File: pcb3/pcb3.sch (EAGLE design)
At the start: 31 parts, among them J1 12V, J2 24V, J3 RTD, J4 RTD, J5 VFS, J6 RELAY, J7 BRAKES, Q1 BSS314PEH6327XTSA1, Q2 BSS314PEH6327XTSA1, Q3 MMBT2222AT-7-F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

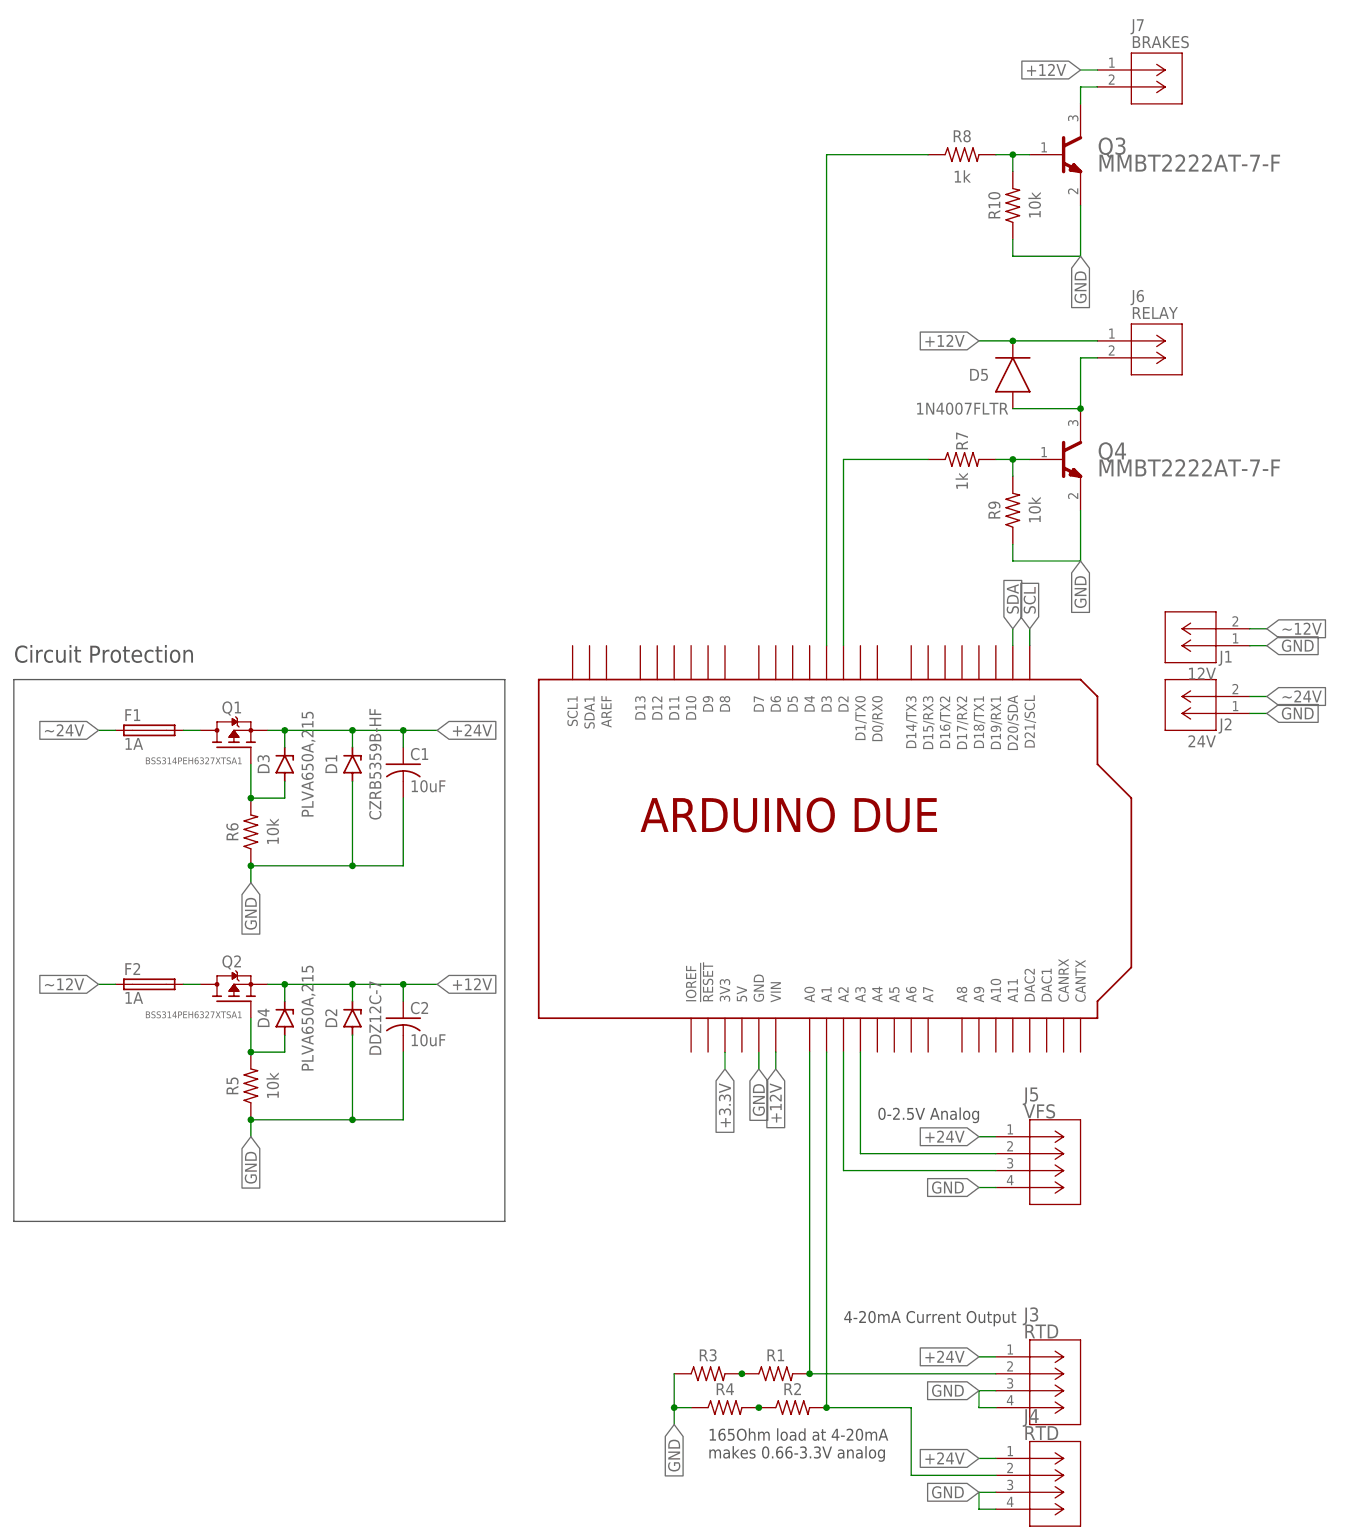
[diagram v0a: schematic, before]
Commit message: Add Serial CAN Bus to PCB 3
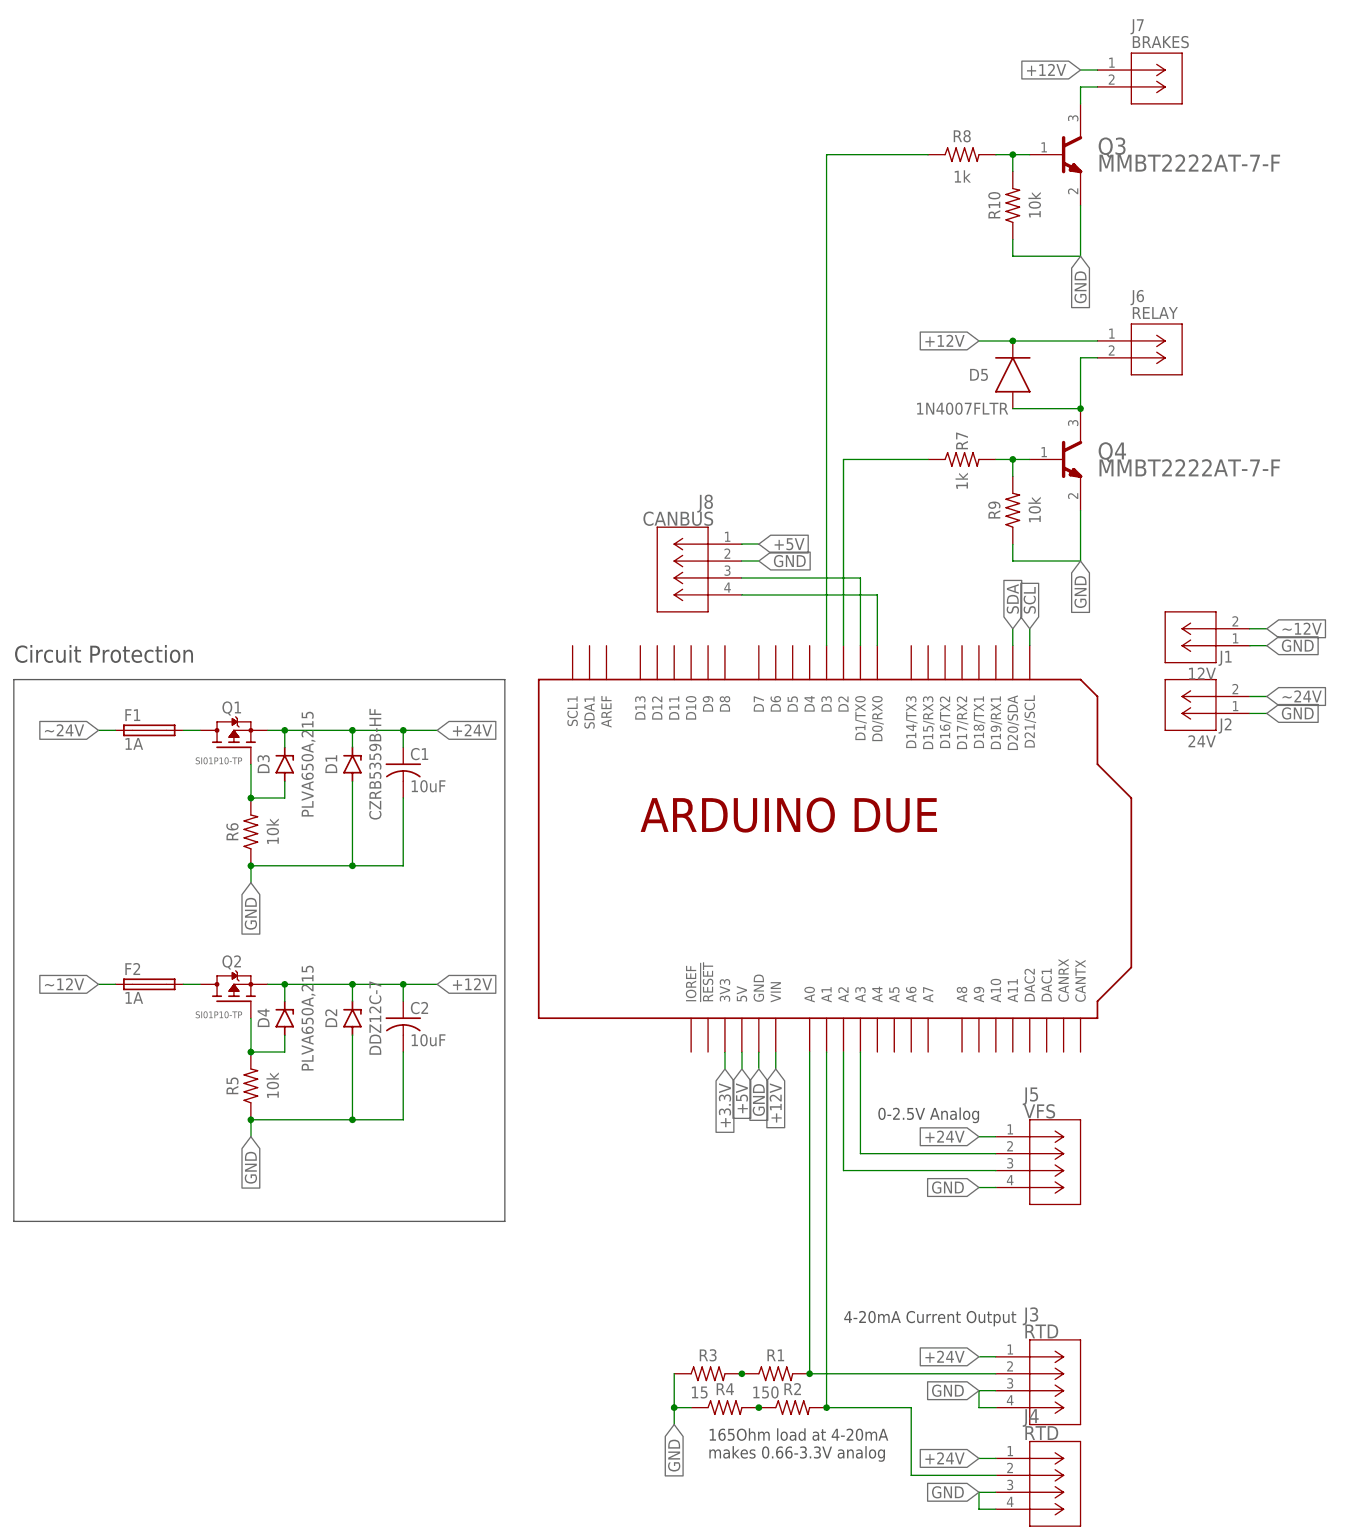
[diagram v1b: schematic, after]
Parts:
- added J8: CANBUS, Molex Micro-Lock PLUS:MICROLOCK-4PIN
- C1, C2: device Capacitor:C-US_CHIP-0603(1608-METRIC) -> Capacitor:C-US_CHIP-1206(3216-METRIC)
- Q1, Q2: value BSS314PEH6327XTSA1 -> SI01P10-TP
- R1, R2: value R-US_CHIP-0603(1608-METRIC) -> 150
- R3, R4: value R-US_CHIP-0603(1608-METRIC) -> 15
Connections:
- new net +5V: J8.1, U$1.5V
- new net N$19: J8.3, U$1.D1/TX0
- new net N$20: J8.4, U$1.D0/RX0
- net GND: now also J8.2
